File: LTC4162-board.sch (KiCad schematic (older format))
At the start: 70 parts, among them J2 Conn_01x02, J3 Conn_02x03_Odd_Even, J4 Conn_01x02, Q1 Q_NMOS_GDS, Q2 Q_NMOS_GDS, U1 LTC4162-L

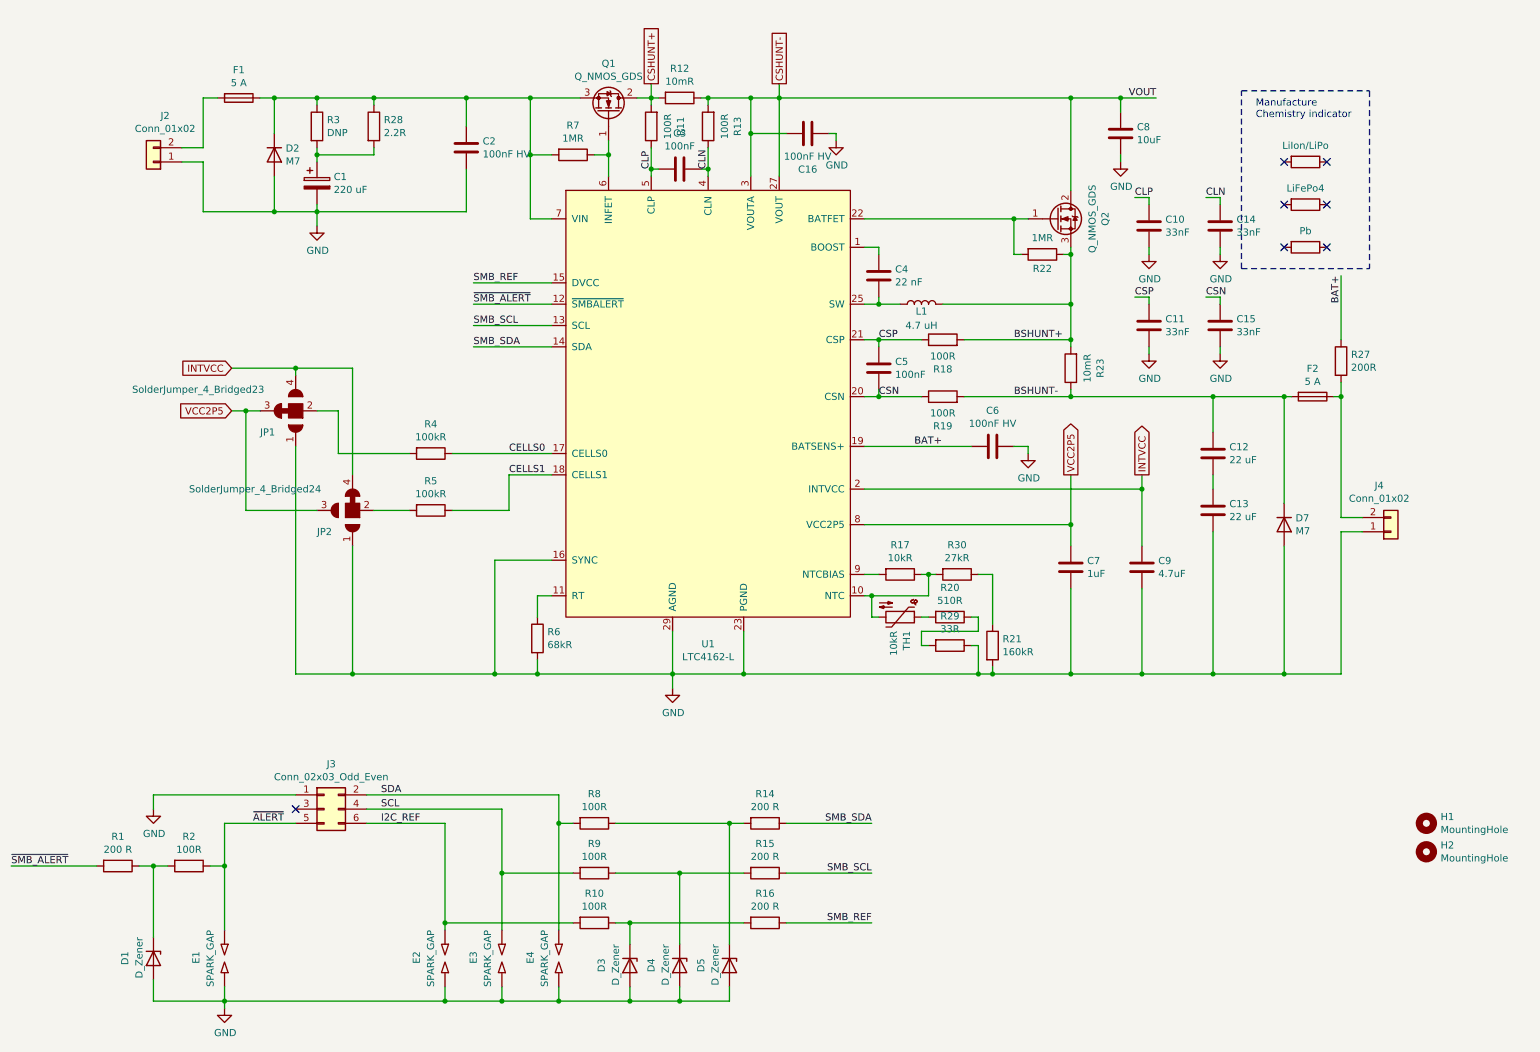
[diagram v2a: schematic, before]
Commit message: Improve bypassing
* Replace input wet electrolytic by solid polymer cap
* Bypass charge output with wet electrolytic
* Bypass both output and batsense+ with 10uF MLCC
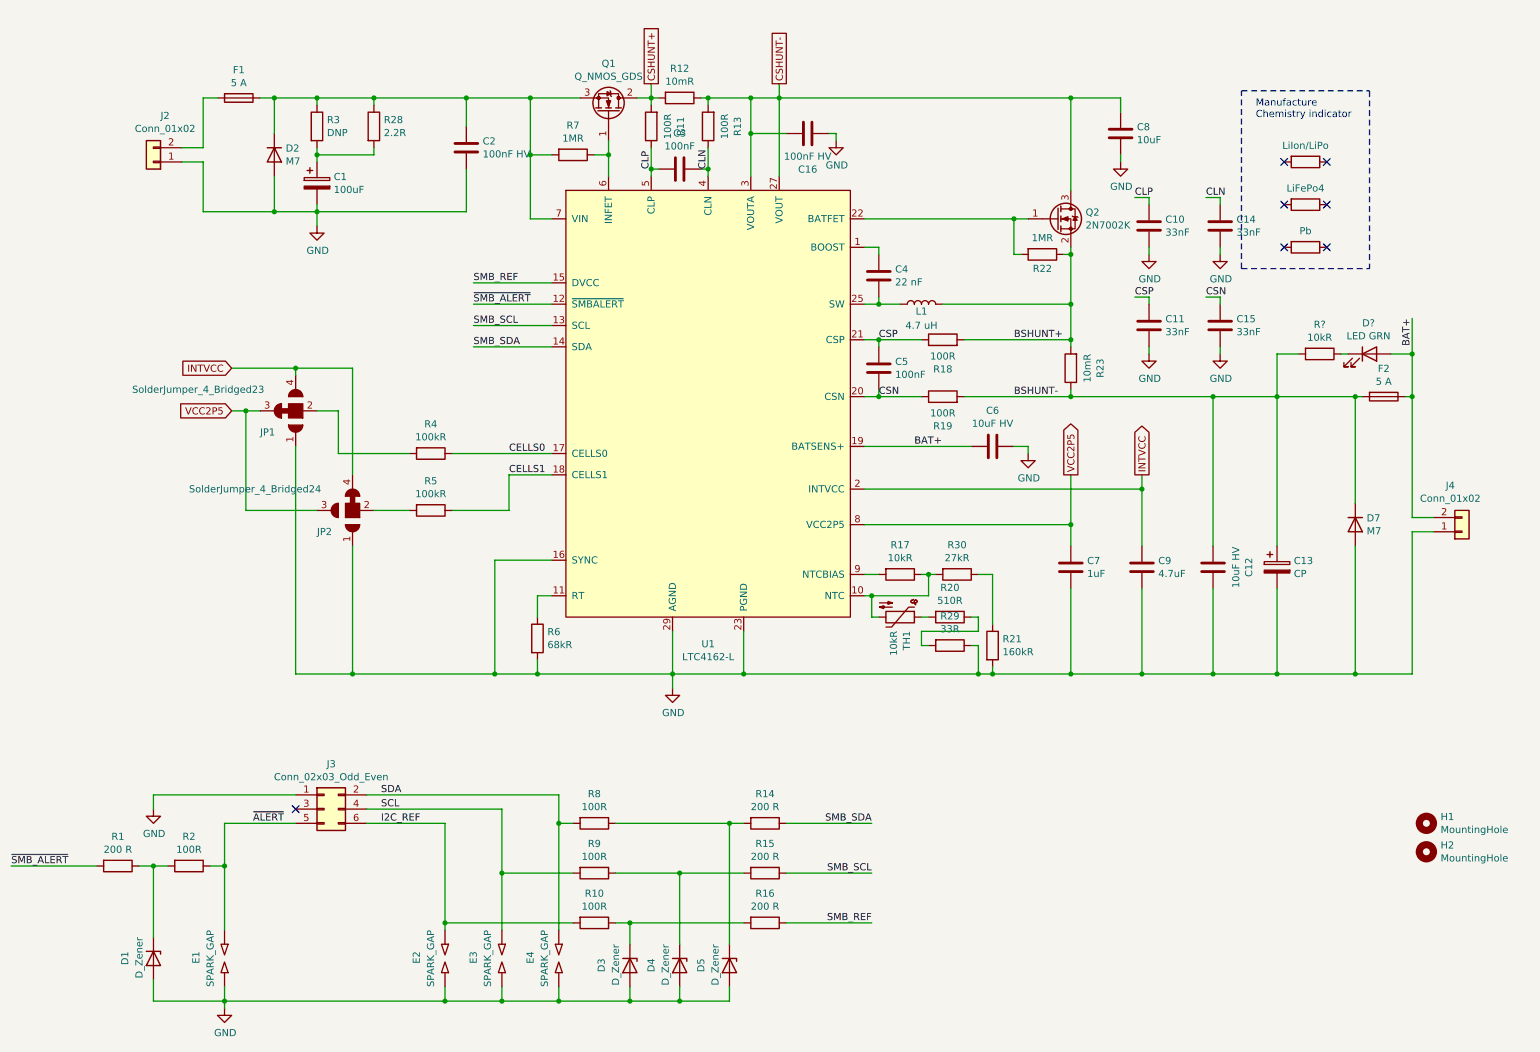
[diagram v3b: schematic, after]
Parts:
- removed C13: 22 uF, Capacitor_SMD:C_0805_2012Metric, symbol Device:C
- removed Q2: Q_NMOS_GDS, Package_TO_SOT_SMD:TO-252-3_TabPin2, symbol Device:Q_NMOS_GDS
- removed R27: 200R, Resistor_SMD:R_0805_2012Metric, symbol Device:R
- added C13: CP, Capacitor_SMD:C_Elec_6.3x7.7, symbol Device:CP
- added D?: LED GRN, LED_SMD:LED_0603_1608Metric, symbol Device:LED
- added Q2: 2N7002K, Package_TO_SOT_SMD:SOT-23, symbol Transistor_FET:2N7002K
- added R?: 10kR, Resistor_SMD:R_0402_1005Metric, symbol Device:R
- C1: value 220 uF -> 100uF; LCSC C125977 -> C249996
- C12: value 22 uF -> 10uF HV; footprint Capacitor_SMD:C_0805_2012Metric -> Capacitor_SMD:C_1206_3216Metric; LCSC C45783 -> C13585
- C6: value 100nF HV -> 10uF HV; footprint Capacitor_SMD:C_0603_1608Metric -> Capacitor_SMD:C_1206_3216Metric; LCSC C14663 -> C13585
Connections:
- net BAT+: now also F2.1, J4.2 (Pin_2), D?.2 (A)
- net BSHUNT+: now also Q2.2 (S)
- net BSHUNT-: now also C13.1, R?.2
- net GND: now also C12.2, C13.2
- net VOUT: now also Q2.3 (D)
- net at R22.2, U1.22 (BATFET): now also Q2.1 (G)
- new net: D?.1 (K), R?.1
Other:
- moved on the sheet: D7, F2, J4
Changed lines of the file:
@@
 AR Path="/602E76F6" Ref="C1"  Part="1"
 F 0 "C1" H 2868 1746 50  0000 L CNN
-F 1 "220 uF" H 2868 1655 50  0000 L CNN
+F 1 "100uF" H 2868 1655 50  0000 L CNN
 F 2 "Capacitor_SMD:CP_Elec_10x10" H 2788 1550 50  0001 C CNN
 F 3 "~" H 2750 1700 50  0001 C CNN
-F 4 "C125977" H 2750 1700 50  0001 C CNN "LCSC"
+F 4 "C249996" H 2750 1700 50  0001 C CNN "LCSC"
 	1    2750 1700
 	1    0    0    -1
@@
 Text GLabel 2150 3000 0    50   Input ~ 0
 INTVCC
-$Comp
-L Device:C C?
-U 1 1 602E7723
-P 9050 3600
-AR Path="/602CD7A6/602E7723" Ref="C?"  Part="1"
-AR Path="/602E7723" Ref="C12"  Part="1"
-F 0 "C12" H 9165 3646 50  0000 L CNN
-F 1 "22 uF" H 9165 3555 50  0000 L CNN
-F 2 "Capacitor_SMD:C_0805_2012Metric" H 9088 3450 50  0001 C CNN
-F 3 "~" H 9050 3600 50  0001 C CNN
-F 4 "C45783" H 9050 3600 50  0001 C CNN "LCSC"
-	1    9050 3600
-	1    0    0    -1
-$EndComp
-Wire Wire Line
-	9050 3450 9050 3200
 $Comp
 L Connector_Generic:Conn_01x02 J?
@@
 Text Label 7650 2800 0    50   ~ 0
 BSHUNT+
-$Comp
-L Device:C C?
-U 1 1 602E7856
-P 9050 4000
-AR Path="/602CD7A6/602E7856" Ref="C?"  Part="1"
-AR Path="/602E7856" Ref="C13"  Part="1"
-F 0 "C13" H 9165 4046 50  0000 L CNN
-F 1 "22 uF" H 9165 3955 50  0000 L CNN
-F 2 "Capacitor_SMD:C_0805_2012Metric" H 9088 3850 50  0001 C CNN
-F 3 "~" H 9050 4000 50  0001 C CNN
-F 4 "C45783" H 9050 4000 50  0001 C CNN "LCSC"
-	1    9050 4000
-	1    0    0    -1
-$EndComp
-Wire Wire Line
-	9050 3850 9050 3750
-Wire Wire Line
-	9050 4150 9050 5150
 Wire Wire Line
 	5800 1100 6000 1100
@@
 AR Path="/602E7878" Ref="C6"  Part="1"
 F 0 "C6" V 7752 3550 50  0000 C CNN
-F 1 "100nF HV" V 7661 3550 50  0000 C CNN
-F 2 "Capacitor_SMD:C_0603_1608Metric" H 7538 3400 50  0001 C CNN
+F 1 "10uF HV" V 7661 3550 50  0000 C CNN
+F 2 "Capacitor_SMD:C_1206_3216Metric" H 7538 3400 50  0001 C CNN
 F 3 "~" H 7500 3550 50  0001 C CNN
-F 4 "C14663" V 7500 3550 50  0001 C CNN "LCSC"
+F 4 "C13585" V 7500 3550 50  0001 C CNN "LCSC"
 	1    7500 3550
 	0    -1   -1   0
@@
 L Device:Fuse F?
 U 1 1 602E78C4
-P 9750 3200
+P 10250 3200
 AR Path="/602CD7A6/602E78C4" Ref="F?"  Part="1"
 AR Path="/602E78C4" Ref="F2"  Part="1"
-F 0 "F2" V 9553 3200 50  0000 C CNN
-F 1 "5 A" V 9644 3200 50  0000 C CNN
-F 2 "Fuse:Fuse_1206_3216Metric" V 9680 3200 50  0001 C CNN
-F 3 "~" H 9750 3200 50  0001 C CNN
-F 4 "C182446" V 9750 3200 50  0001 C CNN "LCSC"
-	1    9750 3200
+F 0 "F2" V 10053 3200 50  0000 C CNN
+F 1 "5 A" V 10144 3200 50  0000 C CNN
+F 2 "Fuse:Fuse_1206_3216Metric" V 10180 3200 50  0001 C CNN
+F 3 "~" H 10250 3200 50  0001 C CNN
+F 4 "C182446" V 10250 3200 50  0001 C CNN "LCSC"
+	1    10250 3200
 	0    1    1    0
 $EndComp
 Wire Wire Line
 	6600 3550 7350 3550
-Text Label 9950 2350 3    50   ~ 0
+Text Label 10450 2650 3    50   ~ 0
 BAT+
 Text Label 6950 3550 0    50   ~ 0
 BAT+
 Wire Wire Line
-	8550 5150 9050 5150
-Wire Wire Line
 	9050 3200 8050 3200
-Connection ~ 9050 3200
 NoConn ~ 9850 1550
 NoConn ~ 9550 1550
@@
 $EndComp
 $Comp
-L Device:Q_NMOS_GDS Q?
-U 1 1 6030636A
-P 7950 1950
-AR Path="/602CD7A6/6030636A" Ref="Q?"  Part="1"
-AR Path="/6030636A" Ref="Q2"  Part="1"
-F 0 "Q2" V 8292 1950 50  0000 C CNN
-F 1 "Q_NMOS_GDS" V 8201 1950 50  0000 C CNN
-F 2 "Package_TO_SOT_SMD:TO-252-3_TabPin2" H 8150 2050 50  0001 C CNN
-F 3 "~" H 7950 1950 50  0001 C CNN
-F 4 "C194346" V 7950 1950 50  0001 C CNN "LCSC"
-	1    7950 1950
-	1    0    0    -1
-$EndComp
-$Comp
 L Device:R R?
 U 1 1 60310CB2
@@
 L Device:D D7
 U 1 1 6031BA3D
-P 9550 4100
-F 0 "D7" V 9504 4180 50  0000 L CNN
-F 1 "M7" V 9595 4180 50  0000 L CNN
-F 2 "Diode_SMD:D_SMA" H 9550 4100 50  0001 C CNN
-F 3 "~" H 9550 4100 50  0001 C CNN
-F 4 "C95872" V 9550 4100 50  0001 C CNN "LCSC"
-	1    9550 4100
-	0    1    1    0
-$EndComp
-Wire Wire Line
-	9550 3950 9550 3200
-Wire Wire Line
-	9050 3200 9550 3200
-Wire Wire Line
-	9550 4250 9550 5150
-Wire Wire Line
-	9550 5150 9050 5150
-Connection ~ 9050 5150
-$Comp
-L Device:R R27
-U 1 1 6036E5F0
-P 9950 2950
-F 0 "R27" H 10020 2996 50  0000 L CNN
-F 1 "200R" H 10020 2905 50  0000 L CNN
-F 2 "Resistor_SMD:R_0805_2012Metric" V 9880 2950 50  0001 C CNN
-F 3 "~" H 9950 2950 50  0001 C CNN
-F 4 "C17540" H 9950 2950 50  0001 C CNN "LCSC"
-	1    9950 2950
-	1    0    0    -1
-$EndComp
-Wire Wire Line
-	9950 3100 9950 3200
-Wire Wire Line
-	9950 2350 9950 2800
-Wire Wire Line
-	8400 1100 8650 1100
-Connection ~ 8400 1100
-Text Label 8650 1100 2    50   ~ 0
-VOUT
+P 10050 4100
+F 0 "D7" V 10004 4180 50  0000 L CNN
+F 1 "M7" V 10095 4180 50  0000 L CNN
+F 2 "Diode_SMD:D_SMA" H 10050 4100 50  0001 C CNN
+F 3 "~" H 10050 4100 50  0001 C CNN
+F 4 "C95872" V 10050 4100 50  0001 C CNN "LCSC"
+	1    10050 4100
+	0    1    1    0
+$EndComp
+Wire Wire Line
+	10050 3950 10050 3200
+Wire Wire Line
+	10050 4250 10050 5150
 $Comp
 L Device:R R20
@@
 L Connector_Generic:Conn_01x02 J?
 U 1 1 605489D0
-P 10300 4150
+P 10800 4150
 AR Path="/602CD7A6/605489D0" Ref="J?"  Part="1"
 AR Path="/605489D0" Ref="J4"  Part="1"
-F 0 "J4" H 10218 3825 50  0000 C CNN
-F 1 "Conn_01x02" H 10218 3916 50  0000 C CNN
-F 2 "Connector_XT:XT60" H 10300 4150 50  0001 C CNN
-F 3 "~" H 10300 4150 50  0001 C CNN
-	1    10300 4150
+F 0 "J4" H 10718 3825 50  0000 C CNN
+F 1 "Conn_01x02" H 10718 3916 50  0000 C CNN
+F 2 "Connector_XT:XT60" H 10800 4150 50  0001 C CNN
+F 3 "~" H 10800 4150 50  0001 C CNN
+	1    10800 4150
 	1    0    0    1
 $EndComp
 Wire Wire Line
-	10100 4150 9950 4150
-Wire Wire Line
-	10100 4050 9950 4050
-Wire Wire Line
-	9900 3200 9950 3200
-Wire Wire Line
-	9600 3200 9550 3200
-Connection ~ 9550 3200
-Connection ~ 9950 3200
-Wire Wire Line
-	9950 5150 9550 5150
-Connection ~ 9550 5150
+	10600 4150 10450 4150
+Wire Wire Line
+	10600 4050 10450 4050
+Wire Wire Line
+	10400 3200 10450 3200
+Wire Wire Line
+	10100 3200 10050 3200
+Connection ~ 10050 3200
+Connection ~ 10450 3200
+Wire Wire Line
+	10450 5150 10050 5150
+Connection ~ 10050 5150
 $Comp
 L Device:R R?
@@
 Connection ~ 7050 4450
 Wire Wire Line
-	9950 4150 9950 5150
-Wire Wire Line
-	9950 3200 9950 4050
+	10450 4150 10450 5150
+Wire Wire Line
+	10450 3200 10450 4050
+$Comp
+L Transistor_FET:2N7002K Q2
+U 1 1 60A64356
+P 7950 1950
+F 0 "Q2" H 8154 1996 50  0000 L CNN
+F 1 "2N7002K" H 8154 1905 50  0000 L CNN
+F 2 "Package_TO_SOT_SMD:SOT-23" H 8150 1875 50  0001 L CIN
+F 3 "https://www.diodes.com/assets/Datasheets/ds30896.pdf" H 7950 1950 50  0001 L CNN
+F 4 "C8545" H 7950 1950 50  0001 C CNN "LCSC"
+	1    7950 1950
+	1    0    0    -1
+$EndComp
+Wire Wire Line
+	10450 2650 10450 2900
+$Comp
+L Device:C C?
+U 1 1 60A9572B
+P 9050 4400
+AR Path="/602CD7A6/60A9572B" Ref="C?"  Part="1"
+AR Path="/60A9572B" Ref="C12"  Part="1"
+F 0 "C12" V 9302 4400 50  0000 C CNN
+F 1 "10uF HV" V 9211 4400 50  0000 C CNN
+F 2 "Capacitor_SMD:C_1206_3216Metric" H 9088 4250 50  0001 C CNN
+F 3 "~" H 9050 4400 50  0001 C CNN
+F 4 "C13585" V 9050 4400 50  0001 C CNN "LCSC"
+	1    9050 4400
+	1    0    0    -1
+$EndComp
+Wire Wire Line
+	8550 5150 9050 5150
+Wire Wire Line
+	9050 3200 9050 4250
+Wire Wire Line
+	9050 4550 9050 5150
+$Comp
+L Device:CP C13
+U 1 1 60ADDBE0
+P 9500 4400
+F 0 "C13" H 9618 4446 50  0000 L CNN
+F 1 "CP" H 9618 4355 50  0000 L CNN
+F 2 "Capacitor_SMD:C_Elec_6.3x7.7" H 9538 4250 50  0001 C CNN
+F 3 "~" H 9500 4400 50  0001 C CNN
+F 4 "C249984" H 9500 4400 50  0001 C CNN "LCSC"
+	1    9500 4400
+	1    0    0    -1
+$EndComp
+Wire Wire Line
+	9500 4250 9500 3200
+Wire Wire Line
+	9500 3200 10050 3200
+Wire Wire Line
+	9050 3200 9500 3200
+Connection ~ 9050 3200
+Connection ~ 9500 3200
+Wire Wire Line
+	9500 4550 9500 5150
+Wire Wire Line
+	9500 5150 10050 5150
+Wire Wire Line
+	9500 5150 9050 5150
+Connection ~ 9500 5150
+Connection ~ 9050 5150
+$Comp
+L Device:LED D?
+U 1 1 60B31D88
+P 10150 2900
+F 0 "D?" H 10143 3117 50  0000 C CNN
+F 1 "LED GRN" H 10143 3026 50  0000 C CNN
+F 2 "LED_SMD:LED_0603_1608Metric" H 10150 2900 50  0001 C CNN
+F 3 "~" H 10150 2900 50  0001 C CNN
+F 4 "C72043" H 10150 2900 50  0001 C CNN "LCSC"
+	1    10150 2900
+	1    0    0    -1
+$EndComp
+$Comp
+L Device:R R?
+U 1 1 60B33209
+P 9800 2900
+F 0 "R?" V 9593 2900 50  0000 C CNN
+F 1 "10kR" V 9684 2900 50  0000 C CNN
+F 2 "Resistor_SMD:R_0402_1005Metric" V 9730 2900 50  0001 C CNN
+F 3 "~" H 9800 2900 50  0001 C CNN
+F 4 "C25744" V 9800 2900 50  0001 C CNN "LCSC"
+	1    9800 2900
+	0    1    1    0
+$EndComp
+Wire Wire Line
+	10300 2900 10450 2900
+Connection ~ 10450 2900
+Wire Wire Line
+	10450 2900 10450 3200
+Wire Wire Line
+	10000 2900 9950 2900
+Wire Wire Line
+	9650 2900 9500 2900
+Wire Wire Line
+	9500 2900 9500 3200
 $EndSCHEMATC
